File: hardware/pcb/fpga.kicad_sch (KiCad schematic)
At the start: 36 parts, among them J200 Conn_02x05_Odd_Even, U200 XC7S25-CSGA225, U201 74LVCH245A

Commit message: - Working on pcb layout
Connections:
- net +1V8_FPGA: no longer C200.2, U200.F9 (VCCADC_0)
- net CRAMA_A0: now also U200.E13 (IO_L18N_T2_15); no longer U200.B13 (IO_L13P_T2_MRCC_15)
- net CRAMA_A1: now also U200.G12 (IO_L23N_T3_15); no longer U200.B14 (IO_L13N_T2_MRCC_15)
- net CRAMA_A10: now also U200.A7 (IO_L3N_T0_DQS_AD1N_15); no longer U200.E12 (IO_L18P_T2_15)
- net CRAMA_A11: now also U200.A6 (IO_L5N_T0_AD2N_15); no longer U200.E13 (IO_L18N_T2_15)
- net CRAMA_A12: now also U200.B13 (IO_L13P_T2_MRCC_15); no longer U200.E14 (IO_L19P_T3_15)
- net CRAMA_A13: now also U200.A12 (IO_L11N_T1_SRCC_AD12N_15); no longer U200.D15 (IO_L19N_T3_VREF_15)
- net CRAMA_A14: now also U200.B11 (IO_L10P_T1_AD4P_15); no longer U200.G15 (IO_L20P_T3_15)
- net CRAMA_A15: now also U200.A11 (IO_L11P_T1_SRCC_AD12P_15); no longer U200.F15 (IO_L20N_T3_15)
- net CRAMA_A16: now also U200.D9 (IO_L7P_T1_AD10P_15); no longer U200.F14 (IO_L21P_T3_DQS_15)
- net CRAMA_A17: now also U200.A10 (IO_L9N_T1_DQS_AD11N_15); no longer U200.E15 (IO_L21N_T3_DQS_15)
- net CRAMA_A18: now also U200.C15 (IO_L14P_T2_SRCC_15); no longer U200.G13 (IO_L22P_T3_15)
- net CRAMA_A19: now also U200.C14 (IO_L15N_T2_DQS_15); no longer U200.G14 (IO_L22N_T3_15)
- net CRAMA_A2: now also U200.G13 (IO_L22P_T3_15); no longer U200.C15 (IO_L14P_T2_SRCC_15)
- net CRAMA_A20: now also U200.A5 (IO_L5P_T0_AD2P_15); no longer U200.G11 (IO_L23P_T3_15)
- net CRAMA_A21: now also U200.D13 (IO_L16N_T2_15); no longer U200.G12 (IO_L23N_T3_15)
- net CRAMA_A3: now also U200.E12 (IO_L18P_T2_15); no longer U200.B15 (IO_L14N_T2_SRCC_15)
- net CRAMA_A4: now also U200.F11 (IO_L17P_T2_15); no longer U200.C13 (IO_L15P_T2_DQS_15)
- net CRAMA_A5: now also U200.C13 (IO_L15P_T2_DQS_15); no longer U200.C14 (IO_L15N_T2_DQS_15)
- net CRAMA_A6: now also U200.C10 (IO_L8P_T1_AD3P_15); no longer U200.D12 (IO_L16P_T2_15)
- net CRAMA_A7: now also U200.B9 (IO_L9P_T1_DQS_AD11P_15); no longer U200.D13 (IO_L16N_T2_15)
- net CRAMA_A8: now also U200.B12 (IO_L10N_T1_AD4N_15); no longer U200.F11 (IO_L17P_T2_15)
- net CRAMA_A9: now also U200.A8 (IO_L6P_T0_15); no longer U200.E11 (IO_L17N_T2_15)
- net CRAMA_ADVN: now also U200.A9 (IO_L6N_T0_VREF_15); no longer U200.A14 (IO_L12N_T1_MRCC_AD5N_15)
- net CRAMA_CEN: now also U200.B10 (IO_L8N_T1_AD3N_15); no longer U200.B11 (IO_L10P_T1_AD4P_15)
- net CRAMA_CRE: now also U200.G11 (IO_L23P_T3_15); no longer U200.A11 (IO_L11P_T1_SRCC_AD12P_15)
- net CRAMA_DQ0: now also U200.D7 (IO_L2P_T0_AD8P_15); no longer U200.D11 (IO_0_15)
- net CRAMA_DQ1: now also U200.D10 (IO_L7N_T1_AD10N_15); no longer U200.C6 (IO_L1P_T0_AD0P_15)
- net CRAMA_DQ10: now also U200.G14 (IO_L22N_T3_15); no longer U200.A6 (IO_L5N_T0_AD2N_15)
- net CRAMA_DQ11: now also U200.E14 (IO_L19P_T3_15); no longer U200.A8 (IO_L6P_T0_15)
- net CRAMA_DQ12: now also U200.E15 (IO_L21N_T3_DQS_15); no longer U200.A9 (IO_L6N_T0_VREF_15)
- net CRAMA_DQ13: now also U200.B14 (IO_L13N_T2_MRCC_15); no longer U200.D9 (IO_L7P_T1_AD10P_15)
- net CRAMA_DQ14: now also U200.D15 (IO_L19N_T3_VREF_15); no longer U200.D10 (IO_L7N_T1_AD10N_15)
- net CRAMA_DQ15: now also U200.B15 (IO_L14N_T2_SRCC_15); no longer U200.C10 (IO_L8P_T1_AD3P_15)
- net CRAMA_DQ2: now also U200.D11 (IO_0_15); no longer U200.C7 (IO_L1N_T0_AD0N_15)
- net CRAMA_DQ3: now also U200.D8 (IO_L2N_T0_AD8N_15); no longer U200.D7 (IO_L2P_T0_AD8P_15)
- net CRAMA_DQ4: now also U200.C9 (IO_L4N_T0_AD9N_15); no longer U200.D8 (IO_L2N_T0_AD8N_15)
- net CRAMA_DQ6: now also U200.C8 (IO_L4P_T0_AD9P_15); no longer U200.A7 (IO_L3N_T0_DQS_AD1N_15)
- net CRAMA_DQ7: now also U200.C6 (IO_L1P_T0_AD0P_15); no longer U200.C8 (IO_L4P_T0_AD9P_15)
- net CRAMA_DQ8: now also U200.F14 (IO_L21P_T3_DQS_15); no longer U200.C9 (IO_L4N_T0_AD9N_15)
- net CRAMA_DQ9: now also U200.F15 (IO_L20N_T3_15); no longer U200.A5 (IO_L5P_T0_AD2P_15)
- net CRAMA_LBN: now also U200.G15 (IO_L20P_T3_15); no longer U200.B10 (IO_L8N_T1_AD3N_15)
- net CRAMA_OEN: now also U200.E11 (IO_L17N_T2_15); no longer U200.A10 (IO_L9N_T1_DQS_AD11N_15)
- net CRAMA_UBN: now also U200.D12 (IO_L16P_T2_15); no longer U200.B9 (IO_L9P_T1_DQS_AD11P_15)
- net CRAMA_WAIT: now also U200.A14 (IO_L12N_T1_MRCC_AD5N_15); no longer U200.A12 (IO_L11N_T1_SRCC_AD12N_15)
- net CRAMA_WEN: now also U200.C7 (IO_L1N_T0_AD0N_15); no longer U200.B12 (IO_L10N_T1_AD4N_15)
- net CRAMB_A0: now also U200.D1 (IO_L6N_T0_VREF_34); no longer U200.H4 (IO_L13P_T2_MRCC_34)
- net CRAMB_A1: now also U200.E1 (IO_L8N_T1_34); no longer U200.H3 (IO_L13N_T2_MRCC_34)
- net CRAMB_A10: now also U200.E3 (IO_L9P_T1_DQS_34); no longer U200.M1 (IO_L18P_T2_34)
- net CRAMB_A11: now also U200.E2 (IO_L8P_T1_34); no longer U200.L1 (IO_L18N_T2_34)
- net CRAMB_A12: now also U200.M3 (IO_L19N_T3_VREF_34); no longer U200.M4 (IO_L19P_T3_34)
- net CRAMB_A13: now also U200.L1 (IO_L18N_T2_34); no longer U200.M3 (IO_L19N_T3_VREF_34)
- net CRAMB_A14: now also U200.N3 (IO_L21N_T3_DQS_34); no longer U200.N2 (IO_L20P_T3_34)
- net CRAMB_A15: now also U200.M1 (IO_L18P_T2_34); no longer U200.M2 (IO_L20N_T3_34)
- net CRAMB_A16: now also U200.H1 (IO_L12P_T1_MRCC_34); no longer U200.P3 (IO_L21P_T3_DQS_34)
- net CRAMB_A17: now also U200.H2 (IO_L14N_T2_SRCC_34); no longer U200.N3 (IO_L21N_T3_DQS_34)
- net CRAMB_A18: now also U200.H4 (IO_L13P_T2_MRCC_34); no longer U200.P1 (IO_L22P_T3_34)
- net CRAMB_A19: now also U200.J3 (IO_L15N_T2_DQS_34); no longer U200.N1 (IO_L22N_T3_34)
- net CRAMB_A2: now also U200.B1 (IO_L4N_T0_34); no longer U200.J2 (IO_L14P_T2_SRCC_34)
- net CRAMB_A20: now also U200.D2 (IO_L6P_T0_34); no longer U200.R4 (IO_L23P_T3_34)
- net CRAMB_A21: now also U200.K1 (IO_L16P_T2_34); no longer U200.R3 (IO_L23N_T3_34)
- net CRAMB_A3: now also U200.J2 (IO_L14P_T2_SRCC_34); no longer U200.H2 (IO_L14N_T2_SRCC_34)
- net CRAMB_A4: now also U200.F1 (IO_L10N_T1_34); no longer U200.J4 (IO_L15P_T2_DQS_34)
- net CRAMB_A5: now also U200.J1 (IO_L16N_T2_34); no longer U200.J3 (IO_L15N_T2_DQS_34)
- net CRAMB_A6: now also U200.K2 (IO_L17N_T2_34); no longer U200.K1 (IO_L16P_T2_34)
- net CRAMB_A7: now also U200.G1 (IO_L12N_T1_MRCC_34); no longer U200.J1 (IO_L16N_T2_34)
- net CRAMB_A8: now also U200.H3 (IO_L13N_T2_MRCC_34); no longer U200.K3 (IO_L17P_T2_34)
- net CRAMB_A9: now also U200.F4 (IO_L11P_T1_SRCC_34); no longer U200.K2 (IO_L17N_T2_34)
- net CRAMB_ADVN: now also U200.D4 (IO_L7P_T1_34); no longer U200.G1 (IO_L12N_T1_MRCC_34)
- net CRAMB_CLK: now also U200.C5 (IO_L5P_T0_34); no longer U200.H1 (IO_L12P_T1_MRCC_34)
- net CRAMB_CRE: now also U200.C1 (IO_L4P_T0_34); no longer U200.F4 (IO_L11P_T1_SRCC_34)
- net CRAMB_DQ0: now also U200.F3 (IO_L11N_T1_SRCC_34); no longer U200.G4 (IO_0_34)
- net CRAMB_DQ1: now also U200.A2 (IO_L2N_T0_34); no longer U200.A4 (IO_L1P_T0_34)
- net CRAMB_DQ10: now also U200.P2 (IO_L24N_T3_34); no longer U200.B5 (IO_L5N_T0_34)
- net CRAMB_DQ11: now also U200.N2 (IO_L20P_T3_34); no longer U200.D2 (IO_L6P_T0_34)
- net CRAMB_DQ12: now also U200.N1 (IO_L22N_T3_34); no longer U200.D1 (IO_L6N_T0_VREF_34)
- net CRAMB_DQ13: now also U200.M4 (IO_L19P_T3_34); no longer U200.D4 (IO_L7P_T1_34)
- net CRAMB_DQ14: now also U200.M2 (IO_L20N_T3_34); no longer U200.C4 (IO_L7N_T1_34)
- net CRAMB_DQ15: now also U200.J4 (IO_L15P_T2_DQS_34); no longer U200.E2 (IO_L8P_T1_34)
- net CRAMB_DQ2: now also U200.B2 (IO_L2P_T0_34); no longer U200.A3 (IO_L1N_T0_34)
- net CRAMB_DQ3: now also U200.A3 (IO_L1N_T0_34); no longer U200.B2 (IO_L2P_T0_34)
- net CRAMB_DQ4: now also U200.A4 (IO_L1P_T0_34); no longer U200.A2 (IO_L2N_T0_34)
- net CRAMB_DQ7: now also U200.B5 (IO_L5N_T0_34); no longer U200.C1 (IO_L4P_T0_34)
- net CRAMB_DQ8: now also U200.P3 (IO_L21P_T3_DQS_34); no longer U200.B1 (IO_L4N_T0_34)
- net CRAMB_DQ9: now also U200.P1 (IO_L22P_T3_34); no longer U200.C5 (IO_L5P_T0_34)
- net CRAMB_LBN: now also U200.R4 (IO_L23P_T3_34); no longer U200.E1 (IO_L8N_T1_34)
- net CRAMB_OEN: now also U200.R3 (IO_L23N_T3_34); no longer U200.D3 (IO_L9N_T1_DQS_34)
- net CRAMB_UBN: now also U200.R2 (IO_L24P_T3_34); no longer U200.E3 (IO_L9P_T1_DQS_34)
- net CRAMB_WAIT: now also U200.G4 (IO_0_34); no longer U200.F3 (IO_L11N_T1_SRCC_34)
- net CRAMB_WEN: now also U200.C4 (IO_L7N_T1_34); no longer U200.F1 (IO_L10N_T1_34)
- net CSI_D0: now also U200.P11 (IO_L16N_T2_D31_14); no longer U200.M9 (IO_L13P_T2_MRCC_14)
- net CSI_D1: now also U200.R9 (IO_L17P_T2_D30_14); no longer U200.M10 (IO_L13N_T2_MRCC_14)
- net CSI_D10: now also U200.M8 (IO_L19N_T3_D25_VREF_14); no longer U200.R11 (IO_L18P_T2_D28_14)
- net CSI_D11: now also U200.N7 (IO_L20N_T3_D23_14); no longer U200.R12 (IO_L18N_T2_D27_14)
- net CSI_D13: now also U200.P10 (IO_L16P_T2_CSI_B_14); no longer U200.M8 (IO_L19N_T3_D25_VREF_14)
- net CSI_D15: now also U200.N11 (IO_L15N_T2_DQS_DOUT_CSO_B_14); no longer U200.N7 (IO_L20N_T3_D23_14)
- net CSI_D2: now also U200.R12 (IO_L18N_T2_D27_14); no longer U200.N12 (IO_L14P_T2_SRCC_14)
- net CSI_D3: now also U200.R11 (IO_L18P_T2_D28_14); no longer U200.P12 (IO_L14N_T2_SRCC_14)
- net CSI_D4: now also U200.P12 (IO_L14N_T2_SRCC_14); no longer U200.N10 (IO_L15P_T2_DQS_RDWR_B_14)
- net CSI_D5: now also U200.N12 (IO_L14P_T2_SRCC_14); no longer U200.N11 (IO_L15N_T2_DQS_DOUT_CSO_B_14)
- net CSI_D6: now also U200.M9 (IO_L13P_T2_MRCC_14); no longer U200.P10 (IO_L16P_T2_CSI_B_14)
- net CSI_D7: now also U200.P7 (IO_L23N_T3_D18_14); no longer U200.P11 (IO_L16N_T2_D31_14)
- net CSI_D8: now also U200.M10 (IO_L13N_T2_MRCC_14); no longer U200.R9 (IO_L17P_T2_D30_14)
- net CSI_D9: now also U200.P6 (IO_L23P_T3_D19_14); no longer U200.R10 (IO_L17N_T2_D29_14)
- net CSI_HSYNC: now also U200.R10 (IO_L17N_T2_D29_14); no longer U200.R5 (IO_L24P_T3_D17_14)
- net CSI_PCLK: now also U200.R5 (IO_L24P_T3_D17_14); no longer U200.P6 (IO_L23P_T3_D19_14)
- net CSI_VSYNC: now also U200.N10 (IO_L15P_T2_DQS_RDWR_B_14); no longer U200.P7 (IO_L23N_T3_D18_14)
- net KEY_DOWN: now also U201.2 (A0); no longer U201.5 (A3)
- net KEY_UP: now also U201.5 (A3); no longer U201.2 (A0)
- net K_A: now also U200.P14 (IO_L11P_T1_SRCC_14); no longer U200.R13 (IO_L12P_T1_MRCC_14)
- net K_DOWN: now also U200.R13 (IO_L12P_T1_MRCC_14), U201.18 (B0); no longer U200.N15 (IO_L10N_T1_D15_14), U201.15 (B3)
- net K_RIGHT: now also U200.M14 (IO_L9P_T1_DQS_14); no longer U200.N14 (IO_L10P_T1_D14_14)
- net K_SELECT: now also U200.N14 (IO_L10P_T1_D14_14); no longer U200.P15 (IO_L11N_T1_SRCC_14)
- net K_START: now also U200.P15 (IO_L11N_T1_SRCC_14); no longer U200.P14 (IO_L11P_T1_SRCC_14)
- net K_UP: now also U200.N15 (IO_L10N_T1_D15_14), U201.15 (B3); no longer U200.M14 (IO_L9P_T1_DQS_14), U201.18 (B0)
- net UART2_RXD: now also U200.M13 (IO_L8P_T1_D11_14)
- net UART2_TXD: now also U200.N13 (IO_L8N_T1_D12_14)
- net SAI4_TX_BCLK: now reaches U200.K14 (IO_L4P_T0_D04_14)
- net SAI4_TX_SYNC: now reaches U200.L14 (IO_L7N_T1_D10_14)
- net SAI4_TX_DATA: now reaches U200.L15 (IO_L4N_T0_D05_14)
- new net: C200.2, U200.F9 (VCCADC_0)
- no-connect marks 3 -> 5
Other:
- moved on the sheet: C200, C201, C202, C203, C204, C205, C206, C207, C208, C209, C210, C211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

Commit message: - PCB r0.3 routed, need to finalize
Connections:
- net +1V8_FPGA: now also C200.2, U200.F9 (VCCADC_0)
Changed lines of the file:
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@@
   (junction (at 45.72 218.44) (diameter 0.9144) (color 0 0 0 0))
   (junction (at 45.72 220.98) (diameter 0.9144) (color 0 0 0 0))
+  (junction (at 58.42 142.24) (diameter 0.9144) (color 0 0 0 0))
   (junction (at 58.42 157.48) (diameter 0.9144) (color 0 0 0 0))
   (junction (at 58.42 160.02) (diameter 0.9144) (color 0 0 0 0))
@@
     (stroke (width 0) (type solid) (color 0 0 0 0))
   )
-  (wire (pts (xy 55.88 142.24) (xy 88.9 142.24))
+  (wire (pts (xy 55.88 142.24) (xy 58.42 142.24))
     (stroke (width 0) (type solid) (color 0 0 0 0))
   )
@@
   )
   (wire (pts (xy 55.88 220.98) (xy 58.42 220.98))
+    (stroke (width 0) (type solid) (color 0 0 0 0))
+  )
+  (wire (pts (xy 58.42 142.24) (xy 88.9 142.24))
     (stroke (width 0) (type solid) (color 0 0 0 0))
   )
@@
       (effects (font (size 1.27 1.27)) (justify left) hide)
     )
+  )
+  (symbol (lib_id "symbols:+1V8_FPGA") (at 58.42 142.24 0) (mirror y) (unit 1)
+    (in_bom yes) (on_board yes)
+    (property "Reference" "#PWR0108" (id 0) (at 58.42 146.05 0)
+      (effects (font (size 1.27 1.27)) hide)
+    )
+    (property "Value" "+1V8_FPGA" (id 1) (at 58.42 138.43 0))
+    (property "Footprint" "" (id 2) (at 58.42 142.24 0)
+      (effects (font (size 1.27 1.27)) hide)
+    )
+    (property "Datasheet" "" (id 3) (at 58.42 142.24 0)
+      (effects (font (size 1.27 1.27)) hide)
+    )
+    (pin "1")
   )
   (symbol (lib_id "symbols:+1V8_FPGA") (at 58.42 157.48 0) (mirror y) (unit 1)
@@
       (effects (font (size 1.27 1.27)) hide)
     )
-    (pin "1")
-  )
-  (symbol (lib_id "symbols:+1V8_FPGA") (at 73.66 71.12 90) (mirror x) (unit 1)
-    (in_bom yes) (on_board yes)
-    (property "Reference" "#PWR0175" (id 0) (at 77.47 71.12 0)
-      (effects (font (size 1.27 1.27)) hide)
-    )
-    (property "Value" "+1V8_FPGA" (id 1) (at 64.77 71.12 90))
-    (property "Footprint" "" (id 2) (at 73.66 71.12 0)
-      (effects (font (size 1.27 1.27)) hide)
-    )
-    (property "Datasheet" "" (id 3) (at 73.66 71.12 0)
-      (effects (font (size 1.27 1.27)) hide)
-    )

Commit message: - PCB layout finished for r0p3
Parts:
- U200: footprint Package_BGA:Xilinx_CSGA225 -> footprint:BGA-225_15x15_13.0x13.0mm
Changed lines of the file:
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@@
       (effects (font (size 1.27 1.27)) (justify left))
     )
-    (property "Footprint" "Package_BGA:Xilinx_CSGA225" (id 2) (at 96.52 205.74 0)
+    (property "Footprint" "footprint:BGA-225_15x15_13.0x13.0mm" (id 2) (at 96.52 205.74 0)
       (effects (font (size 1.27 1.27)) hide)
     )
@@
     (property "Reference" "U200" (id 0) (at 309.88 118.745 0))
     (property "Value" "XC7S25-CSGA225" (id 1) (at 309.88 121.0564 0))
-    (property "Footprint" "Package_BGA:Xilinx_CSGA225" (id 2) (at 309.88 83.82 0)
+    (property "Footprint" "footprint:BGA-225_15x15_13.0x13.0mm" (id 2) (at 309.88 83.82 0)
       (effects (font (size 1.27 1.27)) hide)
     )
@@
     (property "Reference" "U200" (id 0) (at 309.88 220.345 0))
     (property "Value" "XC7S25-CSGA225" (id 1) (at 309.88 222.6564 0))
-    (property "Footprint" "Package_BGA:Xilinx_CSGA225" (id 2) (at 309.88 185.42 0)
+    (property "Footprint" "footprint:BGA-225_15x15_13.0x13.0mm" (id 2) (at 309.88 185.42 0)
       (effects (font (size 1.27 1.27)) hide)
     )
@@
     (property "Reference" "U200" (id 0) (at 119.38 113.665 0))
     (property "Value" "XC7S25-CSGA225" (id 1) (at 119.38 115.9764 0))
-    (property "Footprint" "Package_BGA:Xilinx_CSGA225" (id 2) (at 119.38 78.74 0)
-      (effects (font (size 1.27 1.27)) hide)
-    )
+    (property "Footprint" "footprint:BGA-225_15x15_13.0x13.0mm" (id 2) (at 119.38 78.74 0)
+      (effects (font (size 1.27 1.27)) hide)
+    )

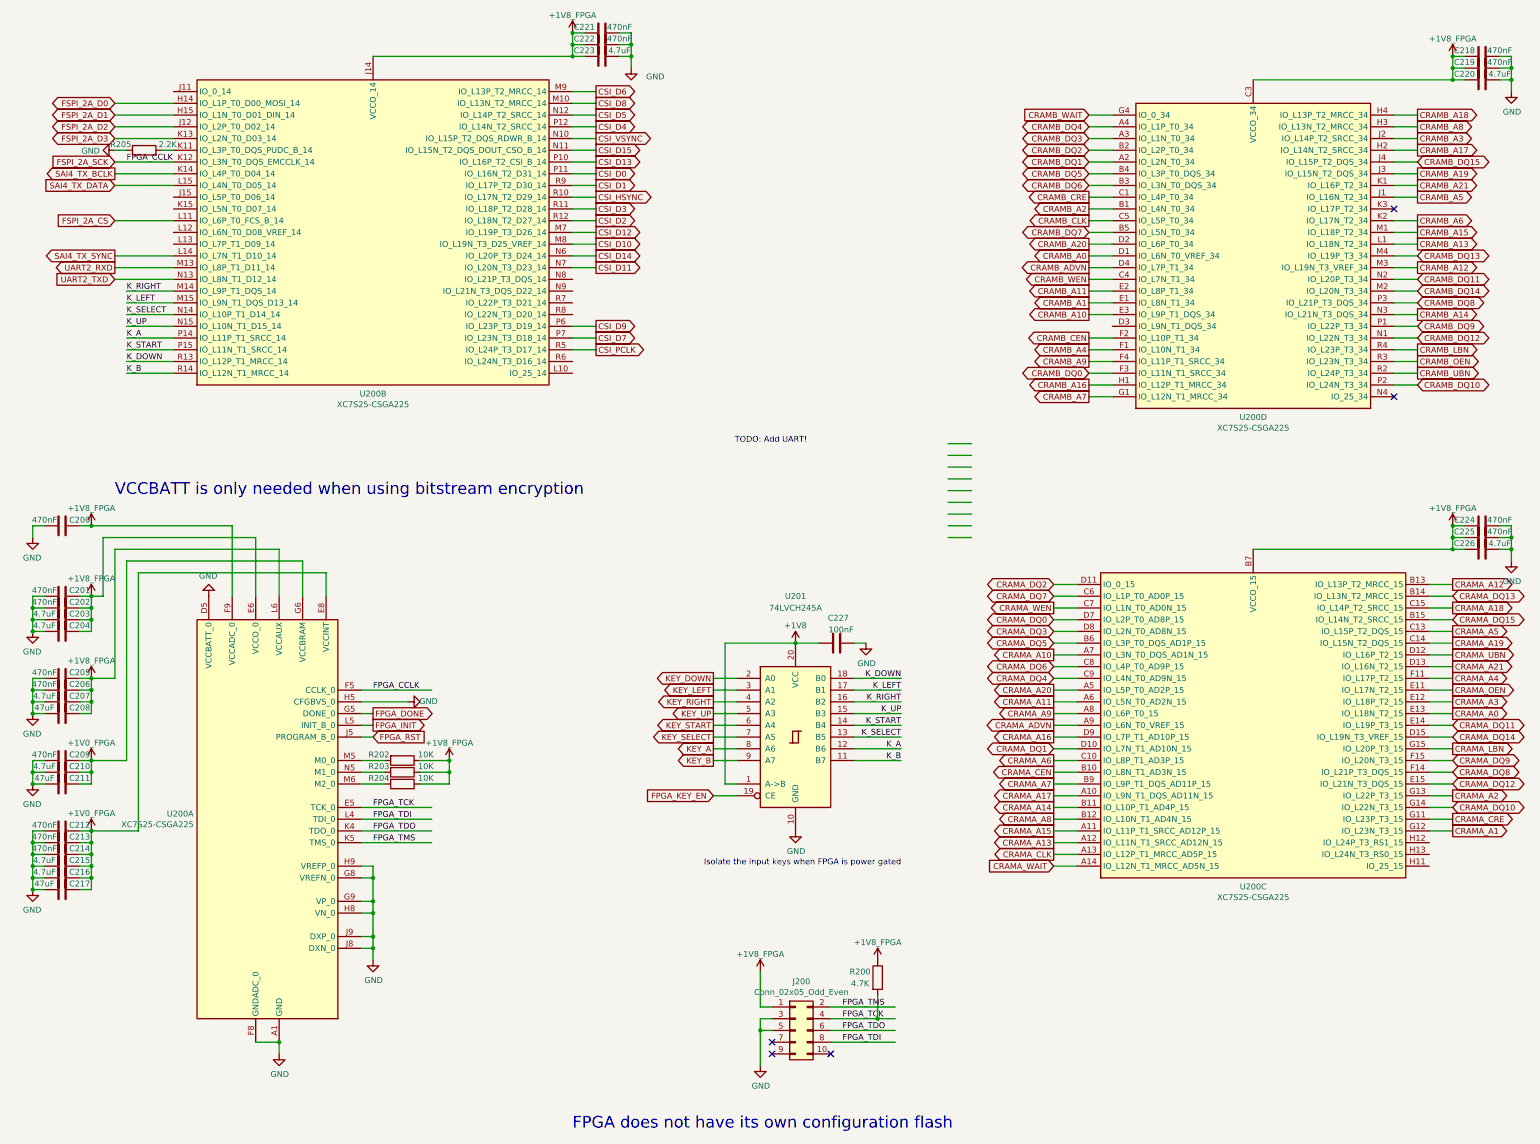
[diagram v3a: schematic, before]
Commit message: - pcb: r0p4, update to KiCAD 6.0
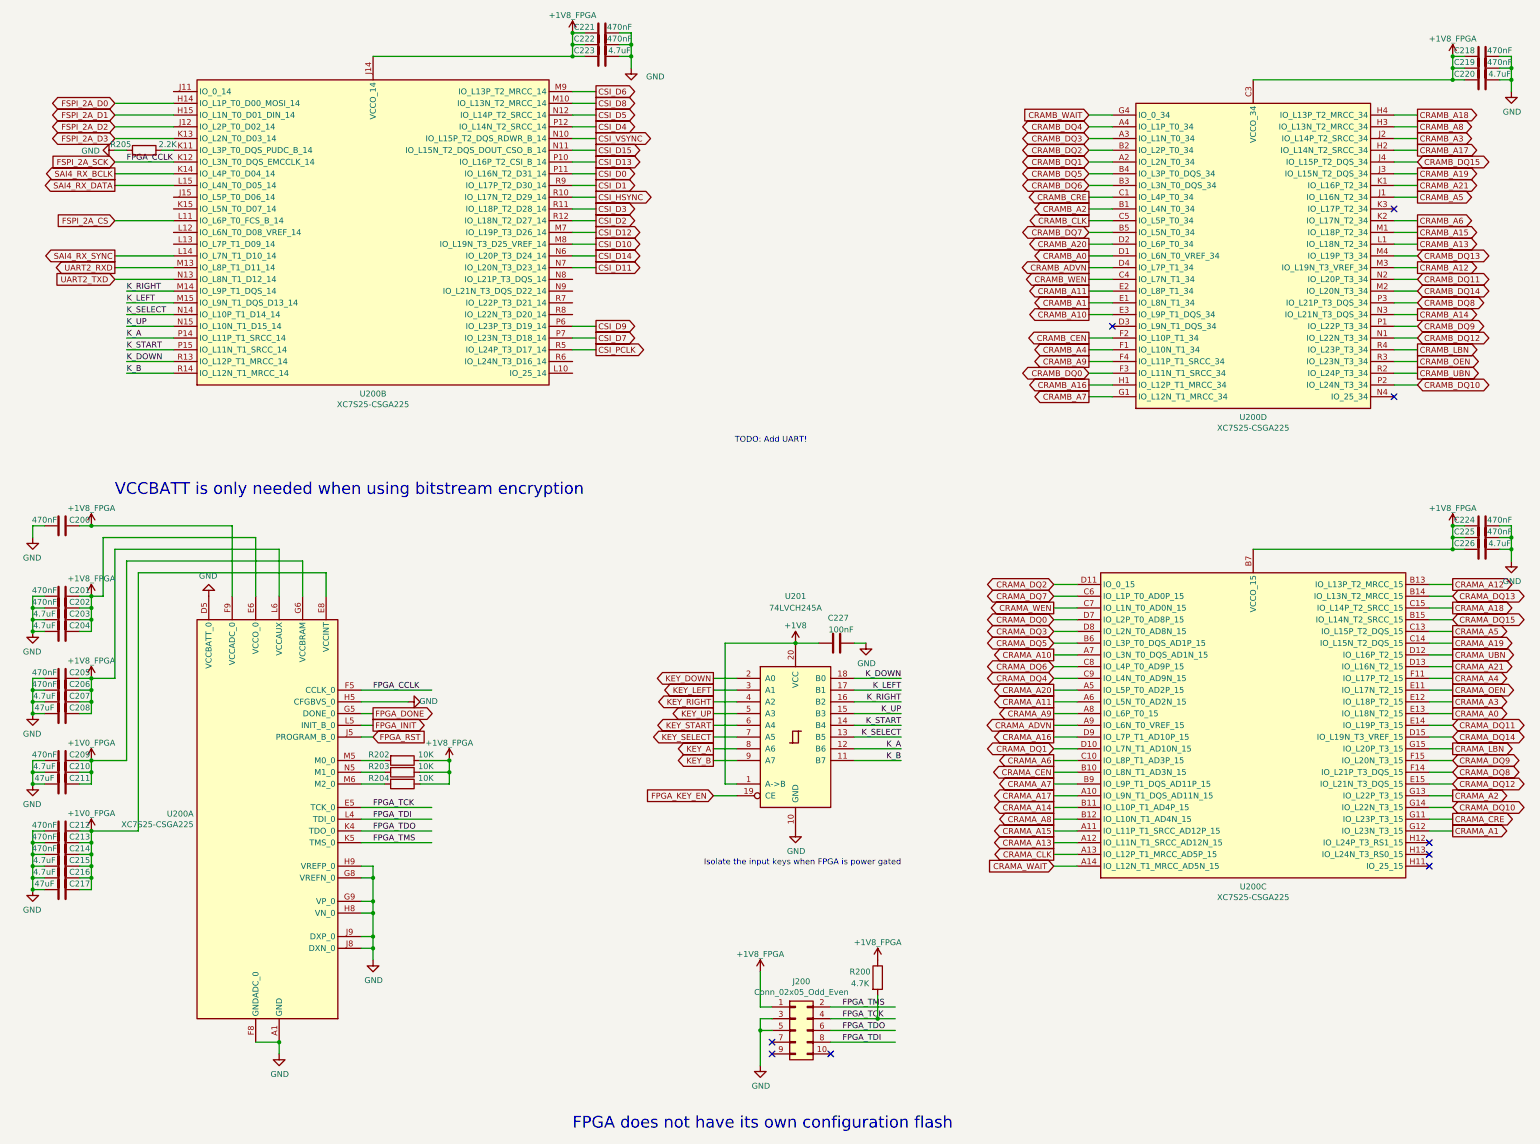
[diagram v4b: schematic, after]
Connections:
- net SAI4_TX_BCLK renamed SAI4_RX_BCLK
- net SAI4_TX_DATA renamed SAI4_RX_DATA
- net SAI4_TX_SYNC renamed SAI4_RX_SYNC
- no-connect marks 5 -> 9
